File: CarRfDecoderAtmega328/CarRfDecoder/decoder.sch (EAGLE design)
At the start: 52 parts, among them T1 BC847, T2 BC847, T3 IRLML6402, U2 RFM69CW, U3 MCP73831, U4 ATMEGA328P, U6 MIC5219 3.3V, Y1 16MHZ

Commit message: bug fixes and better board routing
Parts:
- removed SS: (no value), wirepad:SMD2
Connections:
- removed net AX1: R9A.1, U4.PC2(ADC2)
- removed net AX2: R9B.1, U4.ADC7
- removed net AX3: R9R.1, U4.ADC6
- removed net AX4: R9D.1, U4.PD6(AIN0)
- removed net N$24: AUX4.P, R9D.2
- new net A2: R9D.1, U4.PC2(ADC2)
- new net A6: C4.1, R6D.1, R6R.1, U4.ADC6
- new net A7: R4.1, R5.2, U4.ADC7
- new net D6: R9B.1, U4.PD6(AIN0)
- new net M: AUX1.P, R9D.2
- net A1: now also U3.STAT; no longer R11.1
- net A3: now also R9R.1; no longer C4.1, R6D.1, R6R.1
- net A5: now also R9A.1; no longer R4.1, R5.2
- net D7: now also R11.1; no longer U3.STAT
- net N$21: now also AUX4.P; no longer AUX1.P
- net N$22: now also AUX3.P; no longer AUX2.P
- net N$23: now also AUX2.P; no longer AUX3.P
- net SS: no longer SS.P
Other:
- moved on the sheet: AUX1, AUX2, AUX3, AUX4

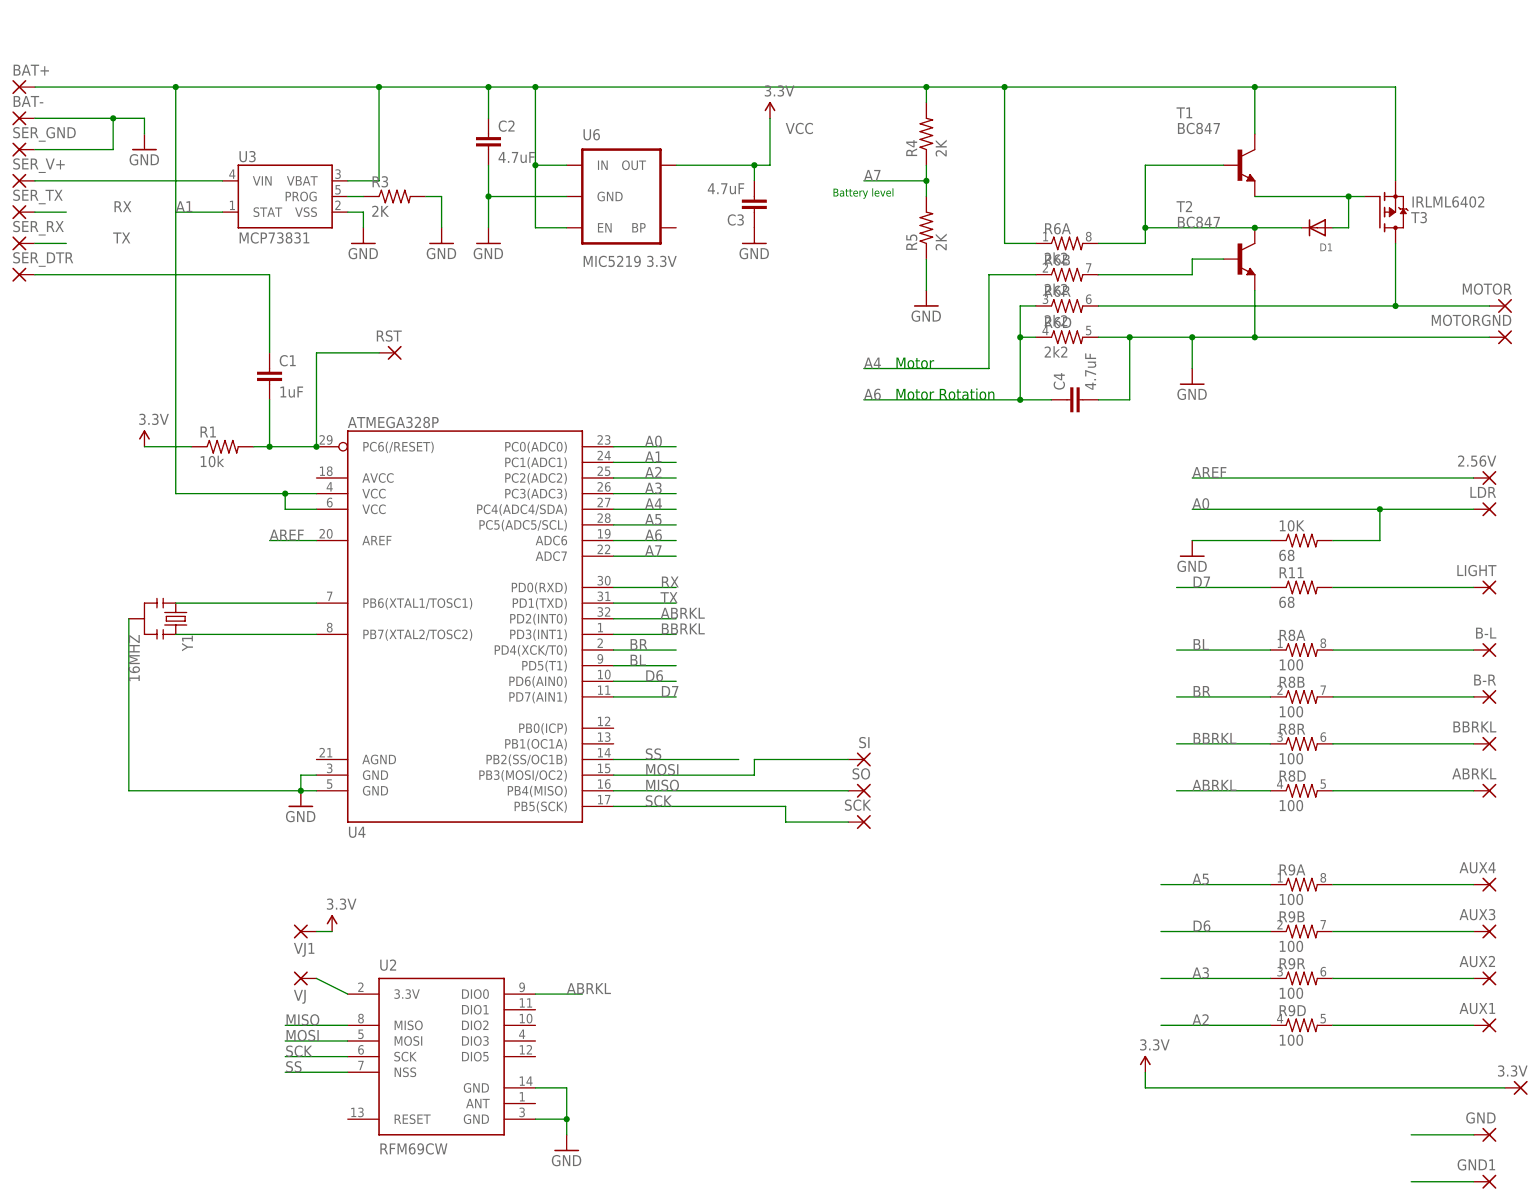
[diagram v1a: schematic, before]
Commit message: Fix light board. Fix carsystem board.
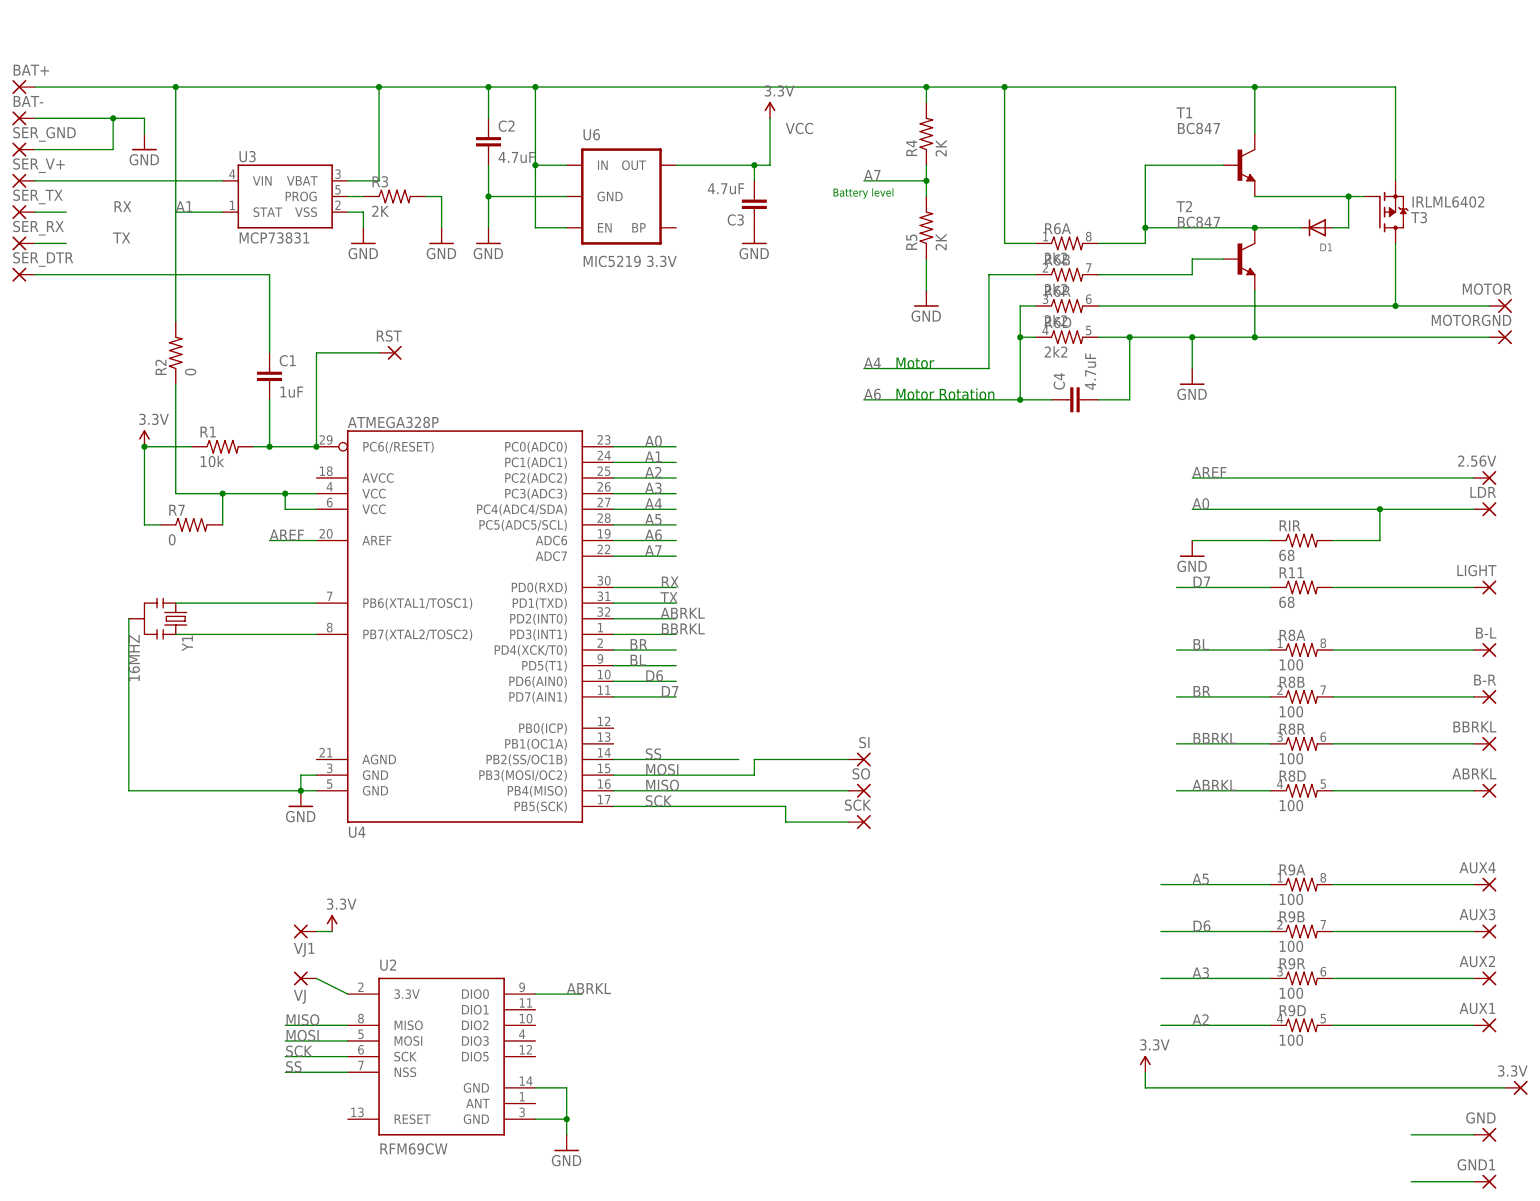
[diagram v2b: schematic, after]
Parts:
- added R2, R7: 0, SparkFun-Resistors:RESISTOR0603-RES
- renumbered 10K to RIR
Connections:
- new net N$6: R2.1, R7.2, U4.VCC@1, U4.VCC@2
- net BAT+: now also R2.2; no longer U4.VCC@1, U4.VCC@2
- net VCC: now also R7.1
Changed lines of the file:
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@@
 <part name="LIGHT" library="wirepad" deviceset="SMD2" device=""/>
 <part name="2.56V" library="wirepad" deviceset="SMD2" device=""/>
-<part name="10K" library="SparkFun-Resistors" deviceset="RESISTOR" device="0603-RES" value="68"/>
+<part name="RIR" library="SparkFun-Resistors" deviceset="RESISTOR" device="0603-RES" value="68"/>
 <part name="LDR" library="wirepad" deviceset="SMD2" device=""/>
 <part name="GND11" library="SparkFun-Aesthetics" deviceset="GND" device=""/>
@@
 <part name="C1" library="SparkFun-Capacitors" deviceset="CAP" device="0805" value="1uF"/>
 <part name="RST" library="wirepad" deviceset="SMD2" device=""/>
+<part name="R2" library="SparkFun-Resistors" deviceset="RESISTOR" device="0603-RES" value="0"/>
+<part name="R7" library="SparkFun-Resistors" deviceset="RESISTOR" device="0603-RES" value="0"/>
 </parts>
 <sheets>
@@
 <instance part="LIGHT" gate="1" x="220.98" y="50.8" rot="MR0"/>
 <instance part="2.56V" gate="1" x="220.98" y="68.58" rot="MR0"/>
-<instance part="10K" gate="G$1" x="190.5" y="58.42"/>
+<instance part="RIR" gate="G$1" x="190.5" y="58.42"/>
 <instance part="LDR" gate="1" x="220.98" y="63.5" rot="MR0"/>
 <instance part="GND11" gate="1" x="172.72" y="55.88"/>
@@
 <instance part="C1" gate="G$1" x="22.86" y="83.82"/>
 <instance part="RST" gate="1" x="43.18" y="88.9" rot="MR0"/>
+<instance part="R2" gate="G$1" x="7.62" y="88.9" rot="R90"/>
+<instance part="R7" gate="G$1" x="10.16" y="60.96"/>
 </instances>
 <busses>
@@
 <wire x1="10.16" y1="73.66" x2="2.54" y2="73.66" width="0.1524" layer="91"/>
 <pinref part="VCC4" gate="G$1" pin="VCC"/>
+<pinref part="R7" gate="G$1" pin="1"/>
+<wire x1="5.08" y1="60.96" x2="2.54" y2="60.96" width="0.1524" layer="91"/>
+<wire x1="2.54" y1="60.96" x2="2.54" y2="73.66" width="0.1524" layer="91"/>
+<junction x="2.54" y="73.66"/>
 </segment>
 </net>
@@
 </segment>
 <segment>
-<pinref part="10K" gate="G$1" pin="1"/>
+<pinref part="RIR" gate="G$1" pin="1"/>
 <wire x1="185.42" y1="58.42" x2="172.72" y2="58.42" width="0.1524" layer="91"/>
 <pinref part="GND11" gate="1" pin="GND"/>
@@
 <pinref part="LDR" gate="1" pin="P"/>
 <wire x1="218.44" y1="63.5" x2="203.2" y2="63.5" width="0.1524" layer="91"/>
-<pinref part="10K" gate="G$1" pin="2"/>
+<pinref part="RIR" gate="G$1" pin="2"/>
 <wire x1="203.2" y1="63.5" x2="172.72" y2="63.5" width="0.1524" layer="91"/>
 <wire x1="195.58" y1="58.42" x2="203.2" y2="58.42" width="0.1524" layer="91"/>
@@
 <net name="BAT+" class="0">
 <segment>
-<pinref part="U4" gate="G$1" pin="VCC@1"/>
-<wire x1="30.48" y1="66.04" x2="25.4" y2="66.04" width="0.1524" layer="91"/>
-<wire x1="25.4" y1="66.04" x2="25.4" y2="63.5" width="0.1524" layer="91"/>
-<pinref part="U4" gate="G$1" pin="VCC@2"/>
-<wire x1="25.4" y1="63.5" x2="30.48" y2="63.5" width="0.1524" layer="91"/>
 <pinref part="U6" gate="G$1" pin="EN"/>
 <wire x1="71.12" y1="109.22" x2="66.04" y2="109.22" width="0.1524" layer="91"/>
@@
 <wire x1="66.04" y1="119.38" x2="71.12" y2="119.38" width="0.1524" layer="91"/>
 <pinref part="BAT+" gate="1" pin="P"/>
+<junction x="40.64" y="132.08"/>
 <wire x1="-15.24" y1="132.08" x2="7.62" y2="132.08" width="0.1524" layer="91"/>
-<junction x="40.64" y="132.08"/>
 <wire x1="7.62" y1="132.08" x2="40.64" y2="132.08" width="0.1524" layer="91"/>
 <wire x1="40.64" y1="132.08" x2="58.42" y2="132.08" width="0.1524" layer="91"/>
@@
 <pinref part="T3" gate="T" pin="S"/>
 <wire x1="205.74" y1="132.08" x2="205.74" y2="116.84" width="0.1524" layer="91"/>
-<wire x1="7.62" y1="132.08" x2="7.62" y2="66.04" width="0.1524" layer="91"/>
+<pinref part="R2" gate="G$1" pin="2"/>
+<wire x1="7.62" y1="93.98" x2="7.62" y2="132.08" width="0.1524" layer="91"/>
 <junction x="7.62" y="132.08"/>
-<wire x1="7.62" y1="66.04" x2="25.4" y2="66.04" width="0.1524" layer="91"/>
-<junction x="25.4" y="66.04"/>
 </segment>
 </net>
@@
 </segment>
 </net>
+<net name="N$6" class="0">
+<segment>
+<pinref part="U4" gate="G$1" pin="VCC@2"/>
+<wire x1="25.4" y1="63.5" x2="30.48" y2="63.5" width="0.1524" layer="91"/>
+<pinref part="U4" gate="G$1" pin="VCC@1"/>
+<wire x1="30.48" y1="66.04" x2="25.4" y2="66.04" width="0.1524" layer="91"/>
+<wire x1="25.4" y1="66.04" x2="25.4" y2="63.5" width="0.1524" layer="91"/>
+<junction x="25.4" y="66.04"/>
+<wire x1="7.62" y1="66.04" x2="15.24" y2="66.04" width="0.1524" layer="91"/>
+<pinref part="R2" gate="G$1" pin="1"/>
+<wire x1="15.24" y1="66.04" x2="25.4" y2="66.04" width="0.1524" layer="91"/>
+<wire x1="7.62" y1="66.04" x2="7.62" y2="83.82" width="0.1524" layer="91"/>
+<pinref part="R7" gate="G$1" pin="2"/>
+<wire x1="15.24" y1="66.04" x2="15.24" y2="60.96" width="0.1524" layer="91"/>
+<junction x="15.24" y="66.04"/>
+</segment>
+</net>

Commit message: CAM file for boards.
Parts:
- renumbered R2 to R_BAT, R7 to R_3.3V
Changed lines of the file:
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@@
 <part name="C1" library="SparkFun-Capacitors" deviceset="CAP" device="0805" value="1uF"/>
 <part name="RST" library="wirepad" deviceset="SMD2" device=""/>
-<part name="R2" library="SparkFun-Resistors" deviceset="RESISTOR" device="0603-RES" value="0"/>
-<part name="R7" library="SparkFun-Resistors" deviceset="RESISTOR" device="0603-RES" value="0"/>
+<part name="R_BAT" library="SparkFun-Resistors" deviceset="RESISTOR" device="0603-RES" value="0"/>
+<part name="R_3.3V" library="SparkFun-Resistors" deviceset="RESISTOR" device="0603-RES" value="0"/>
 </parts>
 <sheets>
@@
 <instance part="C1" gate="G$1" x="22.86" y="83.82"/>
 <instance part="RST" gate="1" x="43.18" y="88.9" rot="MR0"/>
-<instance part="R2" gate="G$1" x="7.62" y="88.9" rot="R90"/>
-<instance part="R7" gate="G$1" x="10.16" y="60.96"/>
+<instance part="R_BAT" gate="G$1" x="7.62" y="88.9" rot="R90"/>
+<instance part="R_3.3V" gate="G$1" x="10.16" y="60.96"/>
 </instances>
 <busses>
@@
 <wire x1="10.16" y1="73.66" x2="2.54" y2="73.66" width="0.1524" layer="91"/>
 <pinref part="VCC4" gate="G$1" pin="VCC"/>
-<pinref part="R7" gate="G$1" pin="1"/>
+<pinref part="R_3.3V" gate="G$1" pin="1"/>
 <wire x1="5.08" y1="60.96" x2="2.54" y2="60.96" width="0.1524" layer="91"/>
 <wire x1="2.54" y1="60.96" x2="2.54" y2="73.66" width="0.1524" layer="91"/>
@@
 <pinref part="T3" gate="T" pin="S"/>
 <wire x1="205.74" y1="132.08" x2="205.74" y2="116.84" width="0.1524" layer="91"/>
-<pinref part="R2" gate="G$1" pin="2"/>
+<pinref part="R_BAT" gate="G$1" pin="2"/>
 <wire x1="7.62" y1="93.98" x2="7.62" y2="132.08" width="0.1524" layer="91"/>
 <junction x="7.62" y="132.08"/>
@@
 <junction x="25.4" y="66.04"/>
 <wire x1="7.62" y1="66.04" x2="15.24" y2="66.04" width="0.1524" layer="91"/>
-<pinref part="R2" gate="G$1" pin="1"/>
+<pinref part="R_BAT" gate="G$1" pin="1"/>
 <wire x1="15.24" y1="66.04" x2="25.4" y2="66.04" width="0.1524" layer="91"/>
 <wire x1="7.62" y1="66.04" x2="7.62" y2="83.82" width="0.1524" layer="91"/>
-<pinref part="R7" gate="G$1" pin="2"/>
+<pinref part="R_3.3V" gate="G$1" pin="2"/>
 <wire x1="15.24" y1="66.04" x2="15.24" y2="60.96" width="0.1524" layer="91"/>
 <junction x="15.24" y="66.04"/>

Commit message: small fixes for vcc.
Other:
- moved on the sheet: R6A, R6B, R6R
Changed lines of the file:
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@@
 <part name="R5" library="SparkFun-Resistors" deviceset="RESISTOR" device="0603-RES" value="2K"/>
 <part name="GND9" library="SparkFun-Aesthetics" deviceset="GND" device=""/>
-<part name="VCC1" library="SparkFun-Aesthetics" deviceset="VCC" device="" value="3.3V"/>
 <part name="R6" library="SparkFun-Resistors" deviceset="RESISTOR-ARRAY" device="0603-ARV" value="2k2"/>
 <part name="R8" library="SparkFun-Resistors" deviceset="RESISTOR-ARRAY" device="0603-ARV" value="100"/>
@@
 <part name="GND11" library="SparkFun-Aesthetics" deviceset="GND" device=""/>
 <part name="3.3V" library="wirepad" deviceset="SMD2" device=""/>
-<part name="VCC2" library="SparkFun-Aesthetics" deviceset="VCC" device="" value="3.3V"/>
 <part name="U2" library="SparkFun-RF" deviceset="RFM69" device="CW"/>
 <part name="GND12" library="SparkFun-Aesthetics" deviceset="GND" device=""/>
-<part name="SUPPLY1" library="SparkFun-Aesthetics" deviceset="VCC" device="" value="3.3V"/>
 <part name="U4" library="SparkFun-DigitalIC" deviceset="ATMEGA328_SMT" device="" value="ATMEGA328P"/>
 <part name="GND3" library="SparkFun-Aesthetics" deviceset="GND" device=""/>
 <part name="SER_GND" library="wirepad" deviceset="SMD2" device=""/>
 <part name="R1" library="SparkFun-Resistors" deviceset="RESISTOR" device="0603-RES" value="10k"/>
-<part name="VCC4" library="SparkFun-Aesthetics" deviceset="VCC" device="" value="3.3V"/>
 <part name="SI" library="wirepad" deviceset="SMD2" device=""/>
 <part name="SO" library="wirepad" deviceset="SMD2" device=""/>
@@
 <instance part="R5" gate="G$1" x="129.54" y="109.22" rot="R90"/>
 <instance part="GND9" gate="1" x="129.54" y="96.52"/>
-<instance part="VCC1" gate="G$1" x="104.14" y="127"/>
-<instance part="R6" gate="A" x="152.4" y="106.68"/>
-<instance part="R6" gate="B" x="152.4" y="101.6"/>
-<instance part="R6" gate="R" x="152.4" y="96.52"/>
+<instance part="R6" gate="A" x="152.4" y="114.3"/>
+<instance part="R6" gate="B" x="152.4" y="106.68"/>
+<instance part="R6" gate="R" x="152.4" y="99.06"/>
 <instance part="R6" gate="D" x="152.4" y="91.44"/>
 <instance part="R8" gate="A" x="190.5" y="40.64"/>
@@
 <instance part="GND11" gate="1" x="172.72" y="55.88"/>
 <instance part="3.3V" gate="1" x="226.06" y="-30.48" rot="MR0"/>
-<instance part="VCC2" gate="G$1" x="165.1" y="-27.94"/>
 <instance part="U2" gate="G$1" x="50.8" y="-25.4"/>
 <instance part="GND12" gate="1" x="71.12" y="-40.64"/>
-<instance part="SUPPLY1" gate="G$1" x="33.02" y="-5.08"/>
 <instance part="U4" gate="G$1" x="53.34" y="48.26"/>
 <instance part="GND3" gate="1" x="27.94" y="15.24"/>
 <instance part="SER_GND" gate="1" x="-17.78" y="121.92"/>
 <instance part="R1" gate="G$1" x="15.24" y="73.66"/>
-<instance part="VCC4" gate="G$1" x="2.54" y="73.66"/>
 <instance part="SI" gate="1" x="119.38" y="22.86" rot="MR0"/>
 <instance part="SO" gate="1" x="119.38" y="17.78" rot="MR0"/>
@@
 <net name="VCC" class="0">
 <segment>
+<pinref part="R1" gate="G$1" pin="1"/>
+<wire x1="10.16" y1="73.66" x2="2.54" y2="73.66" width="0.1524" layer="91"/>
+<pinref part="R_3.3V" gate="G$1" pin="1"/>
+<wire x1="5.08" y1="60.96" x2="2.54" y2="60.96" width="0.1524" layer="91"/>
+<wire x1="2.54" y1="60.96" x2="2.54" y2="73.66" width="0.1524" layer="91"/>
+<wire x1="2.54" y1="73.66" x2="-5.08" y2="73.66" width="0.1524" layer="91"/>
+<junction x="2.54" y="73.66"/>
+<label x="-2.54" y="73.66" size="1.778" layer="95"/>
+</segment>
+<segment>
+<wire x1="165.1" y1="-30.48" x2="223.52" y2="-30.48" width="0.1524" layer="91"/>
+<pinref part="3.3V" gate="1" pin="P"/>
+<label x="165.1" y="-30.48" size="1.778" layer="95"/>
+</segment>
+<segment>
+<pinref part="VJ1" gate="1" pin="P"/>
+<wire x1="33.02" y1="-5.08" x2="30.48" y2="-5.08" width="0.1524" layer="91"/>
+<label x="33.02" y="-5.08" size="1.778" layer="95"/>
+</segment>
+<segment>
 <pinref part="U6" gate="G$1" pin="OUT"/>
 <wire x1="88.9" y1="119.38" x2="101.6" y2="119.38" width="0.1524" layer="91"/>
@@
 <wire x1="104.14" y1="119.38" x2="104.14" y2="127" width="0.1524" layer="91"/>
 <label x="106.68" y="124.46" size="1.778" layer="95"/>
-<pinref part="VCC1" gate="G$1" pin="VCC"/>
 <pinref part="C3" gate="G$1" pin="2"/>
 <wire x1="101.6" y1="116.84" x2="101.6" y2="119.38" width="0.1524" layer="91"/>
 <junction x="101.6" y="119.38"/>
-</segment>
-<segment>
-<wire x1="165.1" y1="-30.48" x2="223.52" y2="-30.48" width="0.1524" layer="91"/>
-<pinref part="3.3V" gate="1" pin="P"/>
-<pinref part="VCC2" gate="G$1" pin="VCC"/>
-<wire x1="165.1" y1="-30.48" x2="165.1" y2="-27.94" width="0.1524" layer="91"/>
-</segment>
-<segment>
-<pinref part="VJ1" gate="1" pin="P"/>
-<pinref part="SUPPLY1" gate="G$1" pin="VCC"/>
-<wire x1="33.02" y1="-5.08" x2="30.48" y2="-5.08" width="0.1524" layer="91"/>
-</segment>
-<segment>
-<pinref part="R1" gate="G$1" pin="1"/>
-<wire x1="10.16" y1="73.66" x2="2.54" y2="73.66" width="0.1524" layer="91"/>
-<pinref part="VCC4" gate="G$1" pin="VCC"/>
-<pinref part="R_3.3V" gate="G$1" pin="1"/>
-<wire x1="5.08" y1="60.96" x2="2.54" y2="60.96" width="0.1524" layer="91"/>
-<wire x1="2.54" y1="60.96" x2="2.54" y2="73.66" width="0.1524" layer="91"/>
-<junction x="2.54" y="73.66"/>
 </segment>
 </net>
@@
 <segment>
 <pinref part="R6" gate="B" pin="1"/>
-<wire x1="147.32" y1="101.6" x2="139.7" y2="101.6" width="0.1524" layer="91"/>
+<wire x1="147.32" y1="106.68" x2="139.7" y2="101.6" width="0.1524" layer="91"/>
 <wire x1="139.7" y1="101.6" x2="139.7" y2="86.36" width="0.1524" layer="91"/>
 <wire x1="139.7" y1="86.36" x2="119.38" y2="86.36" width="0.1524" layer="91"/>
@@
 <segment>
 <pinref part="R6" gate="R" pin="2"/>
-<wire x1="157.48" y1="96.52" x2="205.74" y2="96.52" width="0.1524" layer="91"/>
+<wire x1="157.48" y1="99.06" x2="205.74" y2="96.52" width="0.1524" layer="91"/>
 <pinref part="T3" gate="T" pin="D"/>
 <wire x1="205.74" y1="106.68" x2="205.74" y2="96.52" width="0.1524" layer="91"/>
@@
 <segment>
 <pinref part="R6" gate="B" pin="2"/>
-<wire x1="157.48" y1="101.6" x2="172.72" y2="101.6" width="0.1524" layer="91"/>
+<wire x1="157.48" y1="106.68" x2="172.72" y2="101.6" width="0.1524" layer="91"/>
 <wire x1="172.72" y1="101.6" x2="172.72" y2="104.14" width="0.1524" layer="91"/>
 <pinref part="T2" gate="G$1" pin="B"/>
@@
 <pinref part="R6" gate="A" pin="2"/>
 <wire x1="165.1" y1="109.22" x2="165.1" y2="106.68" width="0.1524" layer="91"/>
-<wire x1="165.1" y1="106.68" x2="157.48" y2="106.68" width="0.1524" layer="91"/>
+<wire x1="165.1" y1="106.68" x2="157.48" y2="114.3" width="0.1524" layer="91"/>
 <wire x1="182.88" y1="109.22" x2="165.1" y2="109.22" width="0.1524" layer="91"/>
 <junction x="182.88" y="109.22"/>
@@
 <junction x="142.24" y="132.08"/>
 <pinref part="R6" gate="A" pin="1"/>
-<wire x1="142.24" y1="106.68" x2="147.32" y2="106.68" width="0.1524" layer="91"/>
+<wire x1="142.24" y1="106.68" x2="147.32" y2="114.3" width="0.1524" layer="91"/>
 <pinref part="T1" gate="G$1" pin="C"/>
 <wire x1="182.88" y1="132.08" x2="182.88" y2="124.46" width="0.1524" layer="91"/>
@@
 <segment>
 <pinref part="R6" gate="R" pin="1"/>
-<wire x1="147.32" y1="96.52" x2="144.78" y2="96.52" width="0.1524" layer="91"/>
+<wire x1="147.32" y1="99.06" x2="144.78" y2="96.52" width="0.1524" layer="91"/>
 <wire x1="144.78" y1="96.52" x2="144.78" y2="91.44" width="0.1524" layer="91"/>
 <pinref part="R6" gate="D" pin="1"/>
